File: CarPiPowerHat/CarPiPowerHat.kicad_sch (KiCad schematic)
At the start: 8 parts, among them J4 Conn_02x03_Counter_Clockwise, J9 Conn_01x04

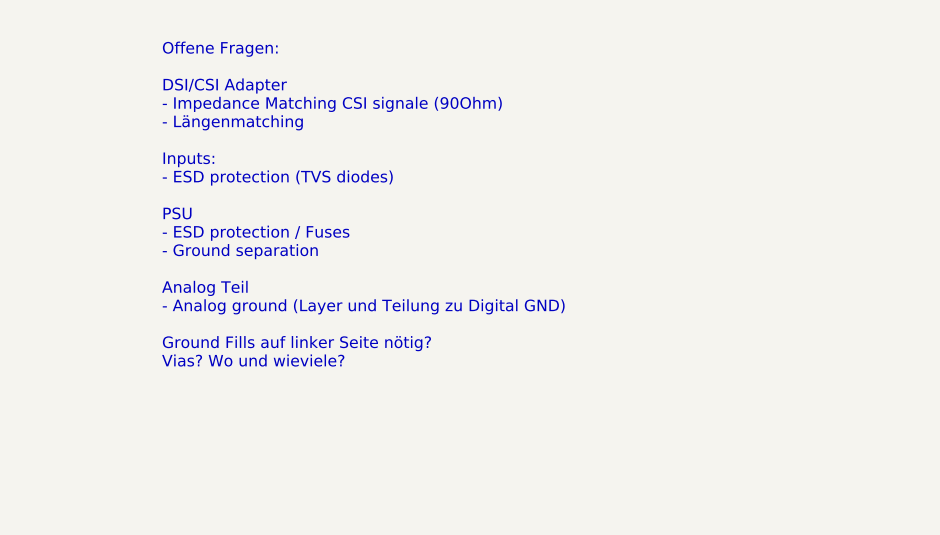
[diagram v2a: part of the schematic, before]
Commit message: Removed TVS diodes for now, fixed DRC issues
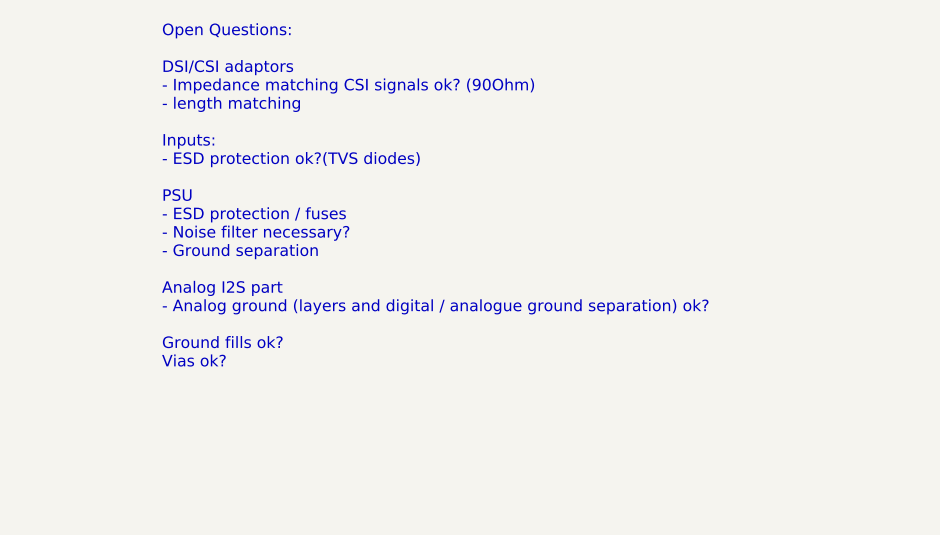
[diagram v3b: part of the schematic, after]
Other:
- note added: "Open Questions: DSI/CSI adaptors - Impedance matching CSI signals ok? (90Ohm) - length matching Inputs: - ESD protection ok?(TVS diodes) PSU - ESD protection / fuses - Noise filter necessary? - Ground separation Analog I2S part - Analog ground (layers and digital / analogue ground separation) ok? Ground fills ok? Vias ok?"
- note removed: "Offene Fragen: DSI/CSI Adapter - Impedance Matching CSI signale (90Ohm) - Längenmatching Inputs: - ESD protection (TVS diodes) PSU - ESD protection / Fuses - Ground separation Analog Teil - Analog ground (Layer und Teilung zu Digital GND) Ground Fills auf linker Seite nötig? Vias? Wo und wieviele?"
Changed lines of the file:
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@@
     (effects (font (size 1.27 1.27)) (justify left bottom))
   )
-  (text "Offene Fragen:\n\nDSI/CSI Adapter\n- Impedance Matching CSI signale (90Ohm)\n- Längenmatching\n\nInputs:\n- ESD protection (TVS diodes)\n\nPSU\n- ESD protection / Fuses\n- Ground separation\n\nAnalog Teil\n- Analog ground (Layer und Teilung zu Digital GND)\n\nGround Fills auf linker Seite nötig?\nVias? Wo und wieviele?\n"
+  (text "Open Questions:\n\nDSI/CSI adaptors\n- Impedance matching CSI signals ok? (90Ohm)\n- length matching\n\nInputs:\n- ESD protection ok?(TVS diodes)\n\nPSU\n- ESD protection / fuses\n- Noise filter necessary?\n- Ground separation\n\nAnalog I2S part\n- Analog ground (layers and digital / analogue ground separation) ok?\n\nGround fills ok?\nVias ok?\n"
     (at 313.69 61.595 0)
     (effects (font (size 1.27 1.27)) (justify left bottom))
@@
       (reference "#PWR01") (unit 1) (value "GND") (footprint "")
     )
-    (path "/d7dab0b1-a885-42c4-b558-97d79e73318c/454a9985-443f-48e2-8597-c05a8aa0e183"
-      (reference "#PWR02") (unit 1) (value "GND") (footprint "")
-    )
     (path "/d7dab0b1-a885-42c4-b558-97d79e73318c/d951192e-ba34-4ff0-b42a-4f774a00b3ca"
       (reference "#PWR0101") (unit 1) (value "GND") (footprint "")
@@
       (reference "D2") (unit 1) (value "LED") (footprint "LED_SMD:LED_0603_1608Metric")
     )
-    (path "/d7dab0b1-a885-42c4-b558-97d79e73318c/2d7884e7-c922-4924-9b7c-055eedf7474e"
-      (reference "D3") (unit 1) (value "D_TVS") (footprint "Diode_SMD:D_SMA_Handsoldering")
-    )
     (path "/d7dab0b1-a885-42c4-b558-97d79e73318c/8bc91e64-556e-4665-9d5b-8482b59816d9"
       (reference "D4") (unit 1) (value "MMBZ5242BLT3G") (footprint "Diode_SMD:D_SOT-23_ANK")
     )
-    (path "/c779e344-5031-4f2d-bf31-77741b3c4be9/3c4a94e7-eac2-4d14-b912-c1f8a8e56573"
-      (reference "D5") (unit 1) (value "D_TVS") (footprint "Diode_SMD:D_SMA_Handsoldering")
-    )
     (path "/c779e344-5031-4f2d-bf31-77741b3c4be9/bd9b82f1-f608-4156-9ed5-b3990567b899"

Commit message: Fixed some bugs, not done yet
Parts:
- renumbered H3 to H1, H1 to H2, H6 to H3, H2 to H5, H5 to H6, J9 to J2, J4 to J6
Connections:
- net +12v: now also J6.4 (Pin_4); no longer J6.1 (Pin_1)
- net CAR_IGN: now also J6.5 (Pin_5); no longer J6.2 (Pin_2)
- net CAR_LIGHT: now also J6.3 (Pin_3); no longer J6.6 (Pin_6)
- net CAR_REVERSE: now also J6.6 (Pin_6); no longer J6.5 (Pin_5)
- net GND: now also J6.1 (Pin_1); no longer J6.3 (Pin_3)
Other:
- added sheet I2S WM8960 (i2s_wm8960.kicad_sch)
- note added: "Connector Car to Board"
- note removed: "Connector Car to Raspberry"
